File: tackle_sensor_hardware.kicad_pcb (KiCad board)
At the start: 4 copper layers, 57.2 x 57.2 mm, 83 parts, among them J1 Conn_01x02_Male, J2 Conn_01x04_Male, J3 Conn_01x03_Male, J4 Conn_ARM_JTAG_SWD_10, Q1 DMP4051LK3, Q2 2N7002K, Q3 2N7002K, Q4 2N7002K, Q5 2N7002K, Q6 2N7002K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

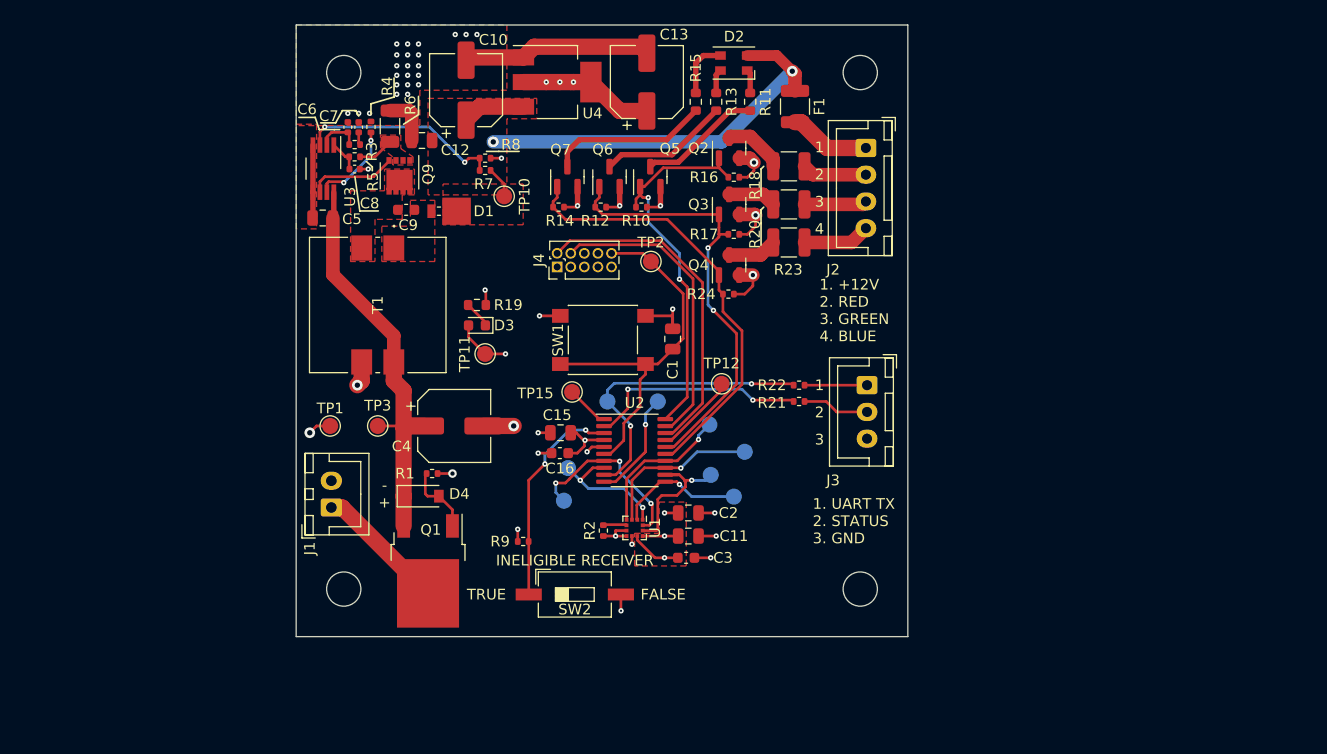
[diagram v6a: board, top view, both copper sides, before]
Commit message: Updating schematic and layout for manufacture with LCSC.
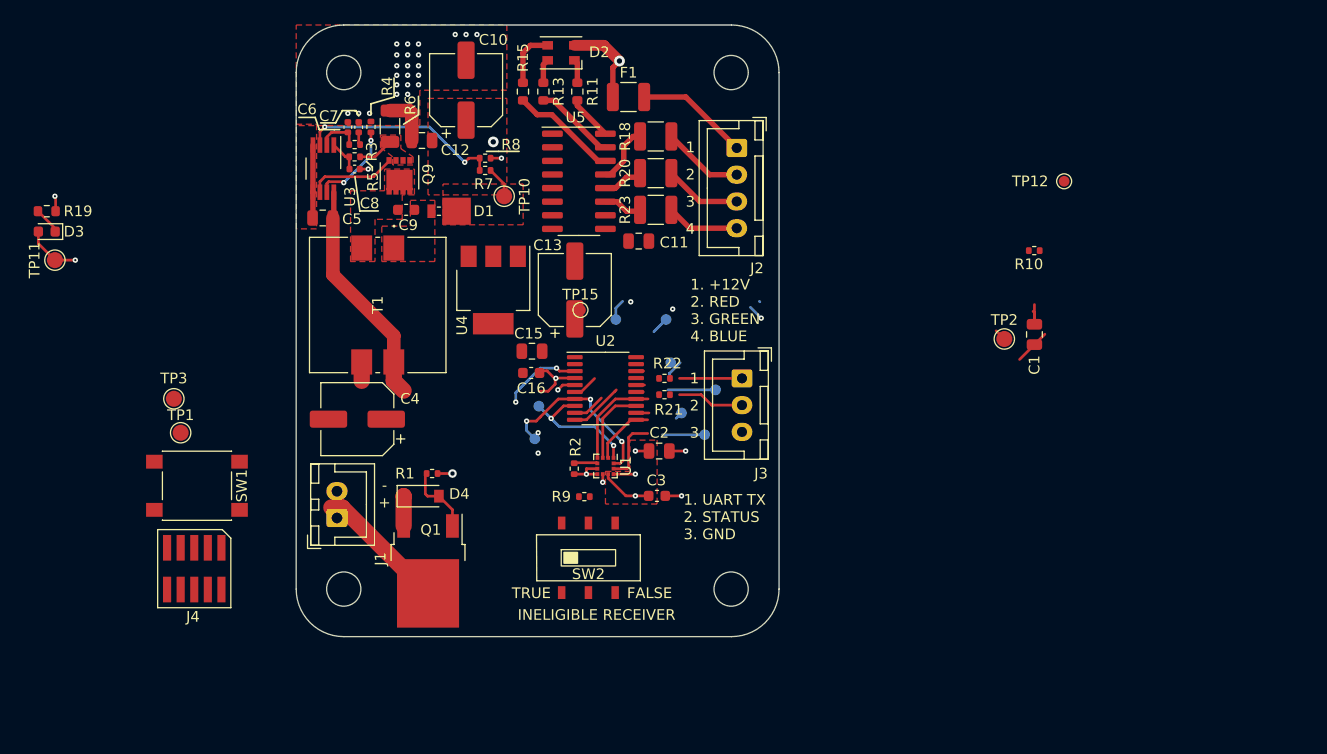
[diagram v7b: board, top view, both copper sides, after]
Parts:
- removed Q2, Q3, Q4, Q5, Q6, Q7: 2N7002K, Package_TO_SOT_SMD:SOT-23
- removed R12, R14, R16, R17, R24: 10k,1%,63mW, Resistor_SMD:R_0402_1005Metric
- added U5: ULN2003ADR, Package_SO:SOIC-16_3.9x9.9mm_P1.27mm, F.Cu at (147.1, 84.5)
- F1: value MF-USHT035KX-2 -> 1210L075YR
- J4: footprint Connector_PinHeader_1.27mm:PinHeader_2x05_P1.27mm_Vertical -> rfc_footprint_lib:20021121-00010C4LF
- SW2: value SW_DIP_x01 -> SW_DPDT_x2; footprint Button_Switch_SMD:SW_DIP_SPSTx01_Slide_6.7x4.1mm_W8.61mm_P2.54mm_LowProfile -> rfc_footprint_lib:SS-3235S-L3
- TP12, TP13, TP14, TP15, TP4, TP5, TP6, TP7, TP8, TP9: footprint TestPoint:TestPoint_Pad_D1.5mm -> TestPoint:TestPoint_Pad_D1.0mm
- moved G*** 51.5 mm to (198.6, 81.0)
- moved J4 44.1 mm to (111.1, 120.7), turned to 180 degrees
- moved D3 41.1 mm to (97.3, 89.2)
- moved R19 41.1 mm to (97.3, 87.2)
- moved TP11 41.1 mm to (98.1, 91.8)
- moved SW1 40.3 mm to (111.4, 112.9), turned to 0 degrees
- moved TP12 37.2 mm to (192.4, 84.5)
- moved R10 36.9 mm to (189.6, 90.9)
- moved TP2 33.8 mm to (186.8, 99.2)
- moved C1 33.8 mm to (189.6, 98.8)
- moved C11 27.9 mm to (152.7, 90.0)
- moved C13 20.6 mm to (146.7, 94.6)
- moved U4 20.3 mm to (139.1, 94.6), turned to -90 degrees
- moved TP3 19.2 mm to (109.2, 104.8)
- moved D2 16.2 mm to (145.4, 72.5)
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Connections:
- C11 pad 1: +3V3 -> +12V
- J1 pad 1: Net-(J1-Pad1) -> GND
- J1 pad 2: GND -> Net-(J1-Pad2)
- Q1 pad 2: Net-(J1-Pad1) -> Net-(J1-Pad2)
- R10 pad 1: R_PWM -> /SWCLK
- SW2 pad 1: Net-(R9-Pad2) -> unconnected-(SW2-Pad1)
- SW2 pad 2: GND -> Net-(R9-Pad2)
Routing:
- net GND: track 85.5 -> 30.3 mm, vias 47 -> 33
- net G_PWM: track 41.5 -> 0.79 mm, vias 2 -> 0
- net B_PWM: track 41.4 -> 0.67 mm
- net R_PWM: track 36.2 -> 0.00 mm, vias 2 -> 0
- net +12V: track 46.3 -> 11.4 mm
- net /SWDIO: track 31.6 -> 0.70 mm
- net /RST: track 35.3 -> 6.80 mm, vias 0 -> 1
- net /SWCLK: track 28.3 -> 0.59 mm, vias 0 -> 1
- net UART_TX: track 28.2 -> 5.27 mm, vias 2 -> 0
- net TACKLE_STATUS: track 20.7 -> 2.20 mm, vias 2 -> 1
- net +3V3: track 34.2 -> 19.1 mm, vias 9 -> 5
- net Net-(C4-Pad1): track 38.6 -> 24.2 mm
- net Net-(R9-Pad2): track 20.3 -> 7.47 mm
- net Net-(J1-Pad2): track 0.00 -> 12.4 mm
- net Net-(J1-Pad1): track 12.4 -> 0.00 mm
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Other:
- board size 57.2 x 57.2 mm -> 45.1 x 57.2 mm

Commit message: updating the BOM
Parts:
- removed the G*** at (198.6, 81.0)
- removed R19: 1k,1%,25mW, Resistor_SMD:R_0603_1608Metric
- removed R20, R23: 0,0.5W, Resistor_SMD:R_1210_3225Metric
- removed R22: 220,1%,63mW, Resistor_SMD:R_0402_1005Metric
- added G***: LOGO, rfc_footprint_lib:new_logo, B.Cu at (143.4, 95.5)
- added G***: LOGO, rfc_footprint_lib:new_logo_highlights, B.Cu at (143.4, 95.5)
- added R12: 1k,1%,25mW, Resistor_SMD:R_0603_1608Metric, F.Cu at (158.1, 91.6)
- added R14: 1k,1%,25mW, Resistor_SMD:R_0603_1608Metric, F.Cu at (158.1, 89.1)
- added R16: 220,1%,63mW, Resistor_SMD:R_0402_1005Metric, F.Cu at (155.2, 77.4)
- added R17: 0,0.5W, Resistor_SMD:R_1210_3225Metric, F.Cu at (156.6, 74.3)
- D1: value SS2PH10HM3_A/H -> DSK34; footprint Diode_SMD:D_Powermite_AK -> Diode_SMD:D_SOD-123F
- Q9: value CSD19538Q3A -> NCE0110K; footprint Package_SON:VSON-8_3.3x3.3mm_P0.65mm_NexFET -> Package_TO_SOT_SMD:TO-252-2
- R15: value 1k,1%,25mW -> 0,0.5W; footprint Resistor_SMD:R_0603_1608Metric -> Resistor_SMD:R_1210_3225Metric
- moved D3 45.9 mm to (141.7, 101.0)
- moved TP11 45.9 mm to (142.5, 103.6)
- moved TP3 45.9 mm to (153.6, 116.6)
- moved TP1 45.9 mm to (154.2, 119.8)
- moved C1 36.7 mm to (154.5, 88.2)
- moved R10 36.7 mm to (154.4, 80.4)
- moved TP12 36.7 mm to (157.2, 73.9)
- moved TP2 36.7 mm to (151.6, 88.6)
- moved J4 30.4 mm to (141.0, 115.1)
- moved Q9 29.2 mm to (156.8, 96.1), turned to 180 degrees
- moved R15 27.6 mm to (157.5, 98.8), turned to 0 degrees
- moved SW1 26.3 mm to (136.9, 106.7)
- moved TP7 24.0 mm to (163.8, 118.0)
- moved TP8 18.7 mm to (154.8, 122.9)
- moved TP6 14.6 mm to (156.5, 118.1)
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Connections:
- Q9 pad 2: Net-(Q9-Pad1) -> Net-(C9-Pad2)
- Q9 pad 3: Net-(Q9-Pad1) -> Net-(Q9-Pad2)
- R10 pad 1: /SWCLK -> Net-(R7-Pad2)
- R13 pad 1: Net-(D2-Pad4) -> Net-(D2-Pad3)
- R13 pad 2: Net-(R13-Pad2) -> Net-(U5-Pad14)
- R15 pad 1: Net-(D2-Pad3) -> Net-(U5-Pad12)
- R15 pad 2: Net-(R15-Pad2) -> Net-(J2-Pad3)
- R5 pad 2: Net-(Q9-Pad1) -> Net-(Q9-Pad2)
- R6 pad 1: Net-(Q9-Pad1) -> Net-(Q9-Pad2)
- R8 pad 1: Net-(R7-Pad2) -> GND
- R8 pad 2: GND -> /SWCLK
- U3 pad 6: Net-(Q9-Pad4) -> Net-(Q9-Pad1)
- U5 pad 12: Net-(R20-Pad1) -> Net-(U5-Pad12)
- U5 pad 14: Net-(R15-Pad2) -> Net-(U5-Pad14)
- U5 pad 15: Net-(R13-Pad2) -> Net-(U5-Pad15)
- U5 pad 7: unconnected-(U5-Pad7) -> GND
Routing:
- net Net-(U5-Pad14): track 0.00 -> 10.0 mm
- net Net-(R15-Pad2): track 10.0 -> 0.00 mm
- net Net-(Q9-Pad4): track 8.31 -> 0.00 mm
- net Net-(U5-Pad15): track 0.00 -> 7.61 mm
- net Net-(R13-Pad2): track 7.61 -> 0.00 mm
- net Net-(Q9-Pad1): track 3.57 -> 8.31 mm
- net Net-(U5-Pad12): track 0.00 -> 3.82 mm
- net Net-(R20-Pad1): track 3.82 -> 0.00 mm
- net Net-(Q9-Pad2): track 0.00 -> 3.57 mm
- net Net-(D2-Pad4): track 2.26 -> 0.00 mm
- net Net-(D2-Pad3): track 5.39 -> 7.65 mm
- net GND: track 30.3 -> 29.4 mm, vias 33 -> 32
- net /SWCLK: track 0.59 -> 1.48 mm
- net Net-(C9-Pad2): vias 0 -> 2
- net /RST: vias 1 -> 0
- added copper zone on B.Cu, net GND
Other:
- board text added: "ELIGIBLE RECEIVER"
- board text removed: "INELIGIBLE RECEIVER"
